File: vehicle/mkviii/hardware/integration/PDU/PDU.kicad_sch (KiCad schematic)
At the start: 44 parts, among them J12 CONN_01X03, J13 CONN_01X03, J14 CONN_01X03, J2 CONN_DSub-9, J6 CONN_01X03, K1 G5Q-1A4-DC5, Q1 SSM3K333R, Q2 SSM3K333R, Q3 SSM3K333R, Q7 SSM3K333R, Q8 SSM3K333R

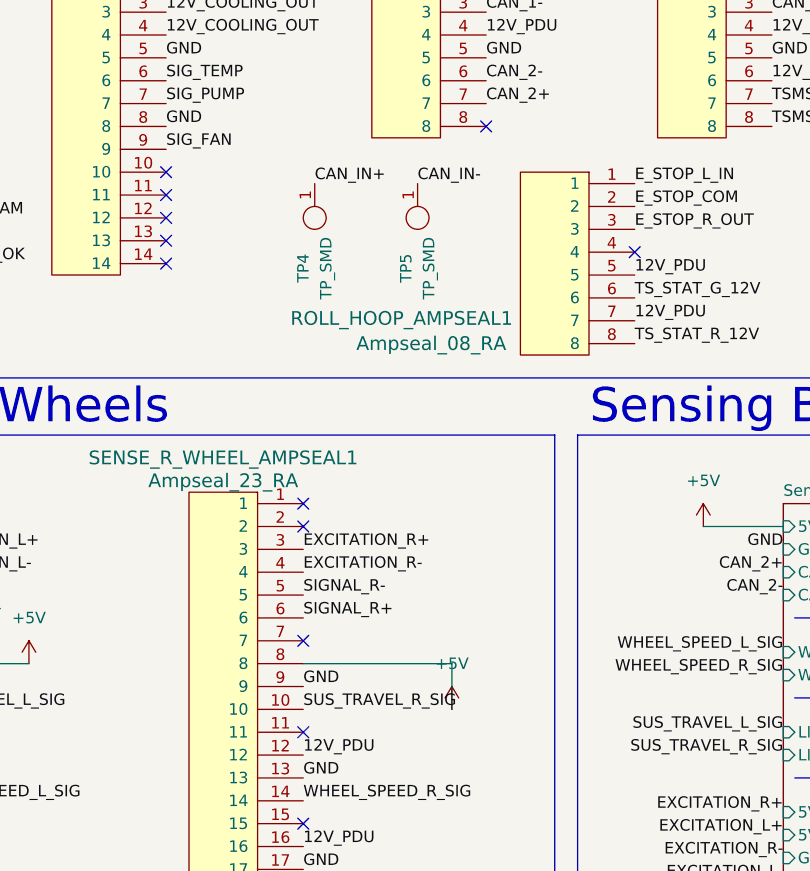
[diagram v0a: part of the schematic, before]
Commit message: Fix CAN test point connection
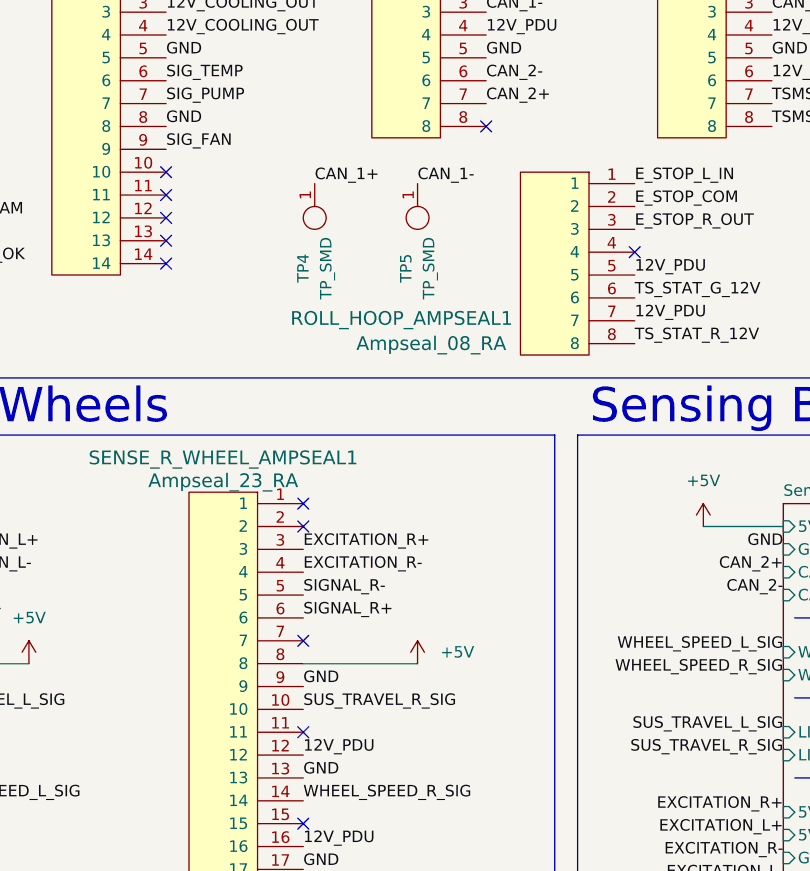
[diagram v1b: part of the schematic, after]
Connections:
- net CAN_IN+ is gone; now on net CAN_1+: TP4.1
- net CAN_IN- is gone; now on net CAN_1-: TP5.1
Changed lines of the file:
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@@
 	(wire
 		(pts
-			(xy 105.41 113.03) (xy 88.9 113.03)
+			(xy 101.6 113.03) (xy 88.9 113.03)
 		)
 		(stroke
@@
 	(wire
 		(pts
-			(xy 105.41 113.03) (xy 105.41 118.11)
-		)
-		(stroke
-			(width 0)
-			(type default)
-		)
-	)
-	(wire
-		(pts
 			(xy 146.05 181.61) (xy 151.13 181.61)
 		)
@@
 		)
 	)
-	(label "CAN_IN-"
+	(label "CAN_1-"
 		(at 101.6 59.69 0)
 		(effects
@@
 		)
 	)
-	(label "CAN_IN+"
+	(label "CAN_1+"
 		(at 90.17 59.69 0)
 		(effects
@@
 	(symbol
 		(lib_id "power:+5V")
-		(at 105.41 118.11 0)
+		(at 101.6 113.03 0)
 		(unit 1)
 		(body_style 1)
@@
 		(fields_autoplaced yes)
 		(property "Reference" "#PWR011"
-			(at 105.41 121.92 0)
+			(at 101.6 116.84 0)
 			(hide yes)
 			(show_name no)
@@
 		)
 		(property "Value" "+5V"
-			(at 105.41 113.03 0)
+			(at 104.14 111.7599 0)
 			(show_name no)
 			(do_not_autoplace no)
@@
 					(size 1.27 1.27)
 				)
+				(justify left)
 			)
 		)
 		(property "Footprint" ""
-			(at 105.41 118.11 0)
+			(at 101.6 113.03 0)
 			(hide yes)
 			(show_name no)
@@
 		)
 		(property "Datasheet" ""
-			(at 105.41 118.11 0)
+			(at 101.6 113.03 0)
 			(hide yes)
 			(show_name no)
@@
 		)
 		(property "Description" "Power symbol creates a global label with name \"+5V\""
-			(at 105.41 118.11 0)
+			(at 101.6 113.03 0)
 			(hide yes)
 			(show_name no)

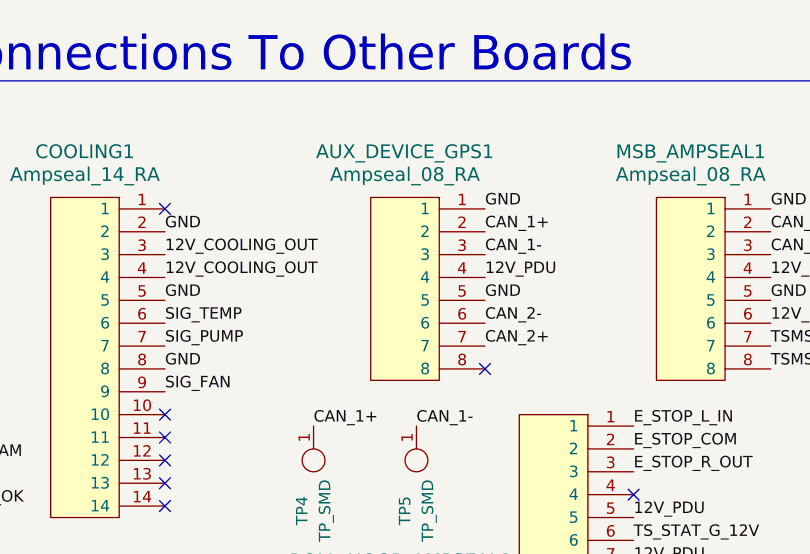
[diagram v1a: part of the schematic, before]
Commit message: Start work on PCB (The parts are placed)
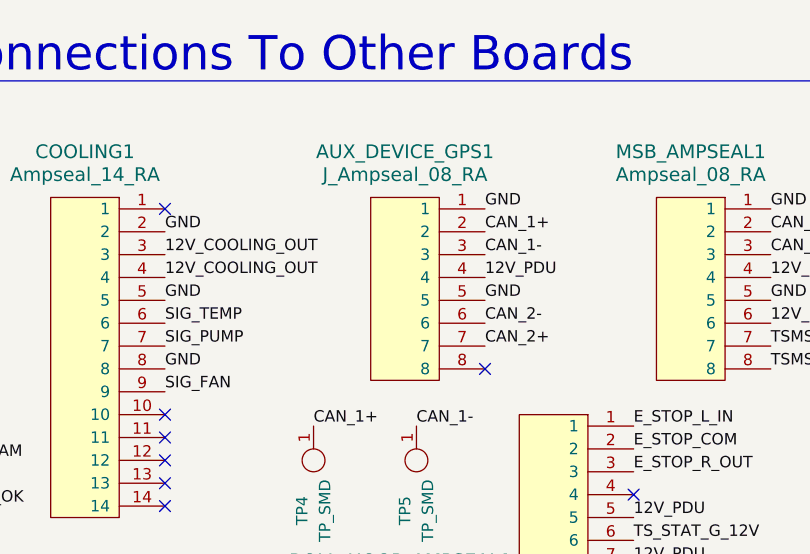
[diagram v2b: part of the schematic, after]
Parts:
- removed AUX_DEVICE_GPS1: Ampseal_08_RA, OEM:J_Ampseal_8_RA, symbol oem:Ampseal_08_RA
- added AUX_DEVICE_GPS1: J_Ampseal_08_RA, OEM:J_Ampseal_8_RA, symbol OEM:J_Ampseal_08_RA
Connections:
- net 12V_PDU: now also AUX_DEVICE_GPS1.4
- net CAN_1+: now also AUX_DEVICE_GPS1.2
- net CAN_1-: now also AUX_DEVICE_GPS1.3
- net CAN_2+: now also AUX_DEVICE_GPS1.7
- net CAN_2-: now also AUX_DEVICE_GPS1.6
- net GND: now also AUX_DEVICE_GPS1.1, AUX_DEVICE_GPS1.5
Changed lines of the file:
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@@
-	)
-	(symbol
-		(lib_id "oem:Ampseal_08_RA")
-		(at 104.14 44.45 0)
-		(unit 1)
-		(body_style 1)
-		(exclude_from_sim no)
-		(in_bom yes)
-		(on_board yes)
-		(in_pos_files yes)
-		(dnp no)
-		(fields_autoplaced yes)
-		(property "Reference" "AUX_DEVICE_GPS1"
-			(at 100.33 29.21 0)
-			(show_name no)
-			(do_not_autoplace no)
-			(effects
-				(font
-					(size 1.524 1.524)
-				)
-			)
-		)
-		(property "Value" "Ampseal_08_RA"
-			(at 100.33 31.75 0)
-			(show_name no)
-			(do_not_autoplace no)
-			(effects
-				(font
-					(size 1.524 1.524)
-				)
-			)
-		)
-		(property "Footprint" "OEM:J_Ampseal_8_RA"
-			(at 99.06 44.45 0)
-			(hide yes)
-			(show_name no)
-			(do_not_autoplace no)
-			(effects
-				(font
-					(size 1.524 1.524)
-				)
-			)
-		)
-		(property "Datasheet" "http://www.te.com/commerce/DocumentDelivery/DDEController?Action=showdoc&DocId=Customer+Drawing%7F776279%7FF7%7Fpdf%7FEnglish%7FENG_CD_776279_F7.pdf%7F1-776279-1"
-			(at 99.06 44.45 0)
-			(hide yes)
-			(show_name no)
-			(do_not_autoplace no)
-			(effects
-				(font
-					(size 1.524 1.524)
-				)
-			)
-		)
-		(property "Description" "Ampseal connector 8 pin right angle"
-			(at 104.14 44.45 0)
-			(hide yes)
-			(show_name no)
-			(do_not_autoplace no)
-			(effects
-				(font
-					(size 1.27 1.27)
-				)
-			)
-		)
-		(property "MFN" "TE"
-			(at 100.33 30.48 0)
-			(hide yes)
-			(show_name no)
-			(do_not_autoplace no)
-			(effects
-				(font
-					(size 1.524 1.524)
-				)
-			)
-		)
-		(property "MPN" "1-776279-1"
-			(at 102.87 27.94 0)
-			(hide yes)
-			(show_name no)
-			(do_not_autoplace no)
-			(effects
-				(font
-					(size 1.524 1.524)
-				)
-			)
-		)
-		(property "PurchasingLink" "http://www.te.com/usa-en/product-1-776279-1.html"
-			(at 105.41 25.4 0)
-			(hide yes)
-			(show_name no)
-			(do_not_autoplace no)
-			(effects
-				(font
-					(size 1.524 1.524)
-				)
-			)
-		)
-		(pin "8"
-		)
-		(pin "1"
-		)
-		(pin "6"
-		)
-		(pin "7"
-		)
-		(pin "4"
-		)
-		(pin "2"
-		)
-		(pin "5"
-		)
-		(pin "3"
-		)
-		(instances
-			(project "PDU"
-				(path "/f655fa78-2860-41ca-ba0e-06d986d434be"
-					(reference "AUX_DEVICE_GPS1")
-					(unit 1)
-				)
-			)
-		)
 	)
 	(symbol
@@
 					(unit 1)
 				)
+			)
+		)
+	)
+	(symbol
+		(lib_id "OEM:J_Ampseal_08_RA")
+		(at 104.14 44.45 0)
+		(unit 1)
+		(body_style 1)
+		(exclude_from_sim no)
+		(in_bom yes)
+		(on_board yes)
+		(in_pos_files yes)
+		(dnp no)
+		(fields_autoplaced yes)
+		(property "Reference" "AUX_DEVICE_GPS1"
+			(at 100.33 29.21 0)
+			(show_name no)
+			(do_not_autoplace no)
+			(effects
+				(font
+					(size 1.524 1.524)
+				)
+			)
+		)
+		(property "Value" "J_Ampseal_08_RA"
+			(at 100.33 31.75 0)
+			(show_name no)
+			(do_not_autoplace no)
+			(effects
+				(font
+					(size 1.524 1.524)
+				)
+			)
+		)
+		(property "Footprint" "OEM:J_Ampseal_8_RA"
+			(at 99.06 44.45 0)
+			(hide yes)
+			(show_name no)
+			(do_not_autoplace no)
+			(effects
+				(font
+					(size 1.524 1.524)
+				)
+			)
+		)
+		(property "Datasheet" "http://www.te.com/commerce/DocumentDelivery/DDEController?Action=showdoc&DocId=Customer+Drawing%7F776279%7FF7%7Fpdf%7FEnglish%7FENG_CD_776279_F7.pdf%7F1-776279-1"
+			(at 99.06 44.45 0)
+			(hide yes)
+			(show_name no)
+			(do_not_autoplace no)
+			(effects
+				(font
+					(size 1.524 1.524)
+				)
+			)
+		)
+		(property "Description" "Ampseal connector 8 pin right angle"
+			(at 104.14 44.45 0)
+			(hide yes)
+			(show_name no)
+			(do_not_autoplace no)
+			(effects
+				(font
+					(size 1.27 1.27)
+				)
+			)
+		)
+		(property "MPN" "1-776279-1"
+			(at 102.87 27.94 0)
+			(hide yes)
+			(show_name no)
+			(do_not_autoplace no)
+			(effects
+				(font
+					(size 1.524 1.524)
+				)
+			)
+		)
+		(pin "4"
+		)
+		(pin "2"
+		)
+		(pin "7"
+		)
+		(pin "5"
+		)
+		(pin "8"
+		)
+		(pin "6"
+		)
+		(pin "3"
+		)
+		(pin "1"
+		)
+		(instances
+			(project "PDU"
+				(path "/f655fa78-2860-41ca-ba0e-06d986d434be"
+					(reference "AUX_DEVICE_GPS1")
+					(unit 1)
+				)

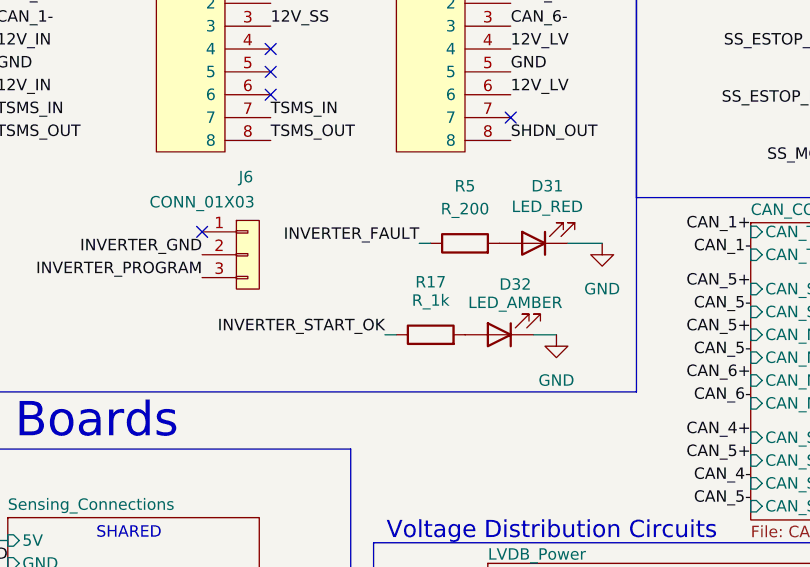
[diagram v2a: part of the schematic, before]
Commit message: Sort the parts together
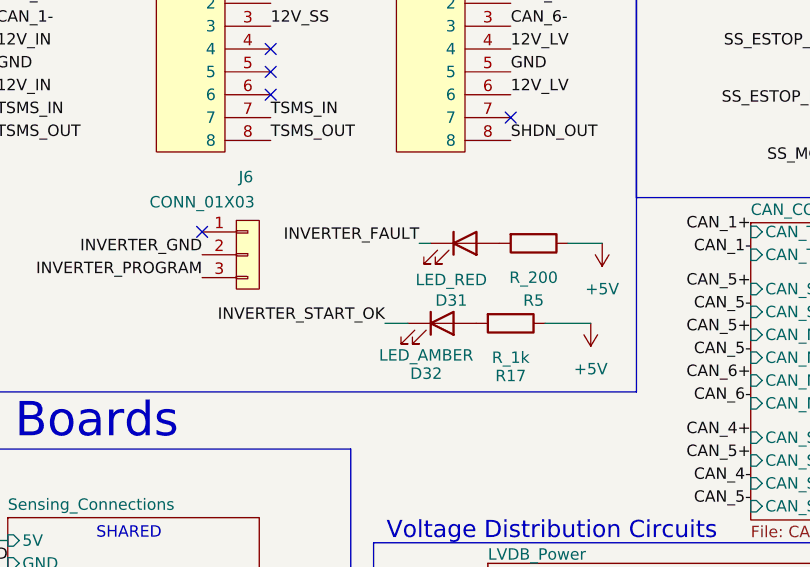
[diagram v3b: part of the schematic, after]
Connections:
- net +5V: now also R17.1, R5.1
- net GND: no longer D31.1 (K), D32.1 (K)
- net INVERTER_FAULT: now also D31.1 (K); no longer R5.1
- net INVERTER_START_OK: now also D32.1 (K); no longer R17.1
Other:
- moved on the sheet: D31, D32, R17, R5
